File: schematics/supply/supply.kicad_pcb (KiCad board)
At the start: 4 copper layers, 237.5 x 175 mm, 293 parts, among them J1 Conn_01x02_Pin, J11 Conn_01x04_Pin, J13 USBASP, J14 USBASP, J15 Conn_01x05_Pin, J17 banana jack + fuse 20A, J18 Conn_02x04_Odd_Even, J19 banana jack + fuse 15A, J2 Conn_01x02_Pin, J20 jst xh angle, J21 jst xh angle, J3 Conn_01x01_Pin, J4 Conn_01x01_Pin, J5 CW2B-10A-T, J6 USB_A, J7 USB_A, J8 USB_A, J9 Conn_01x04_Pin, K1 SRD-12VDC-SL-C, M1 Fan, Q1 STP13NK60Z, Q10 IRLML0030, Q11 IRLML0030, Q12 IRLML0030, Q13 IRLML5203, Q14 IRLML5203, Q2 IRLML5203, Q3 40N06, Q4 STP13NK60Z, Q5 STP13NK60Z, Q6 IRLML0030, Q7 IRLML5203, Q8 IRLML5203, Q9 IRLML0030, SW3 SW_Push, U1 ICE2PCS01, U10 LM158DR, U11 IP2163, U12 LM158DR, U13 TL432DBZ, U14 LM158DR, U15 LDL1117S33R, U16 ATmega328-A, U17 ATtiny1616-M, U19 LM158DR, U2 TL331, U20 EL817, U21 IRS2153S, U22 TL331, U23 INA169, U24 LM1085-3.3, U25 INA3221, U3 R7731, U4 EL817, U5 TL432DBZ, U6 INA3221, U7 EL817, U8 MC34063AD, U9 IRS2153S, X1 CSX-750FCC, 16MHz, X2 HC-49U, 16MHz, Y1 B32022A3223M000

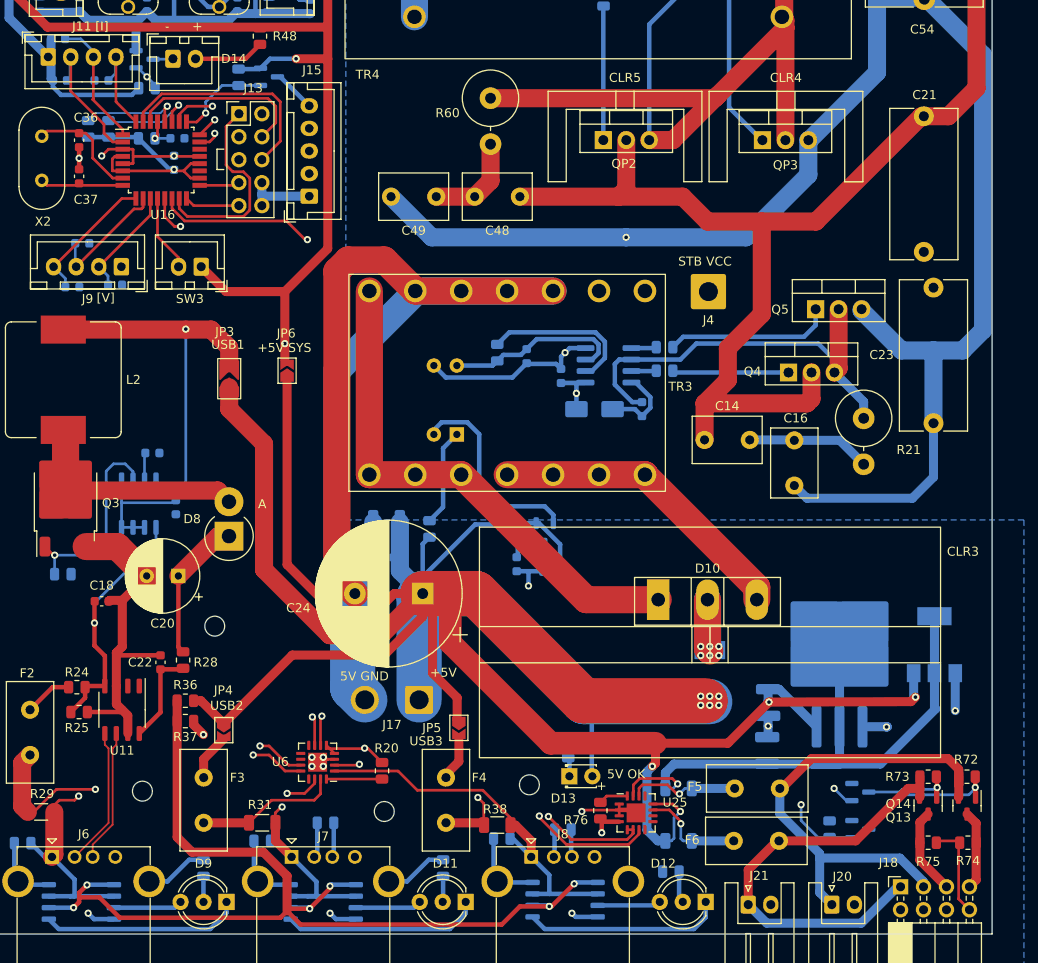
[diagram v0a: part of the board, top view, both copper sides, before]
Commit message: Added over-voltage protection to 5V line
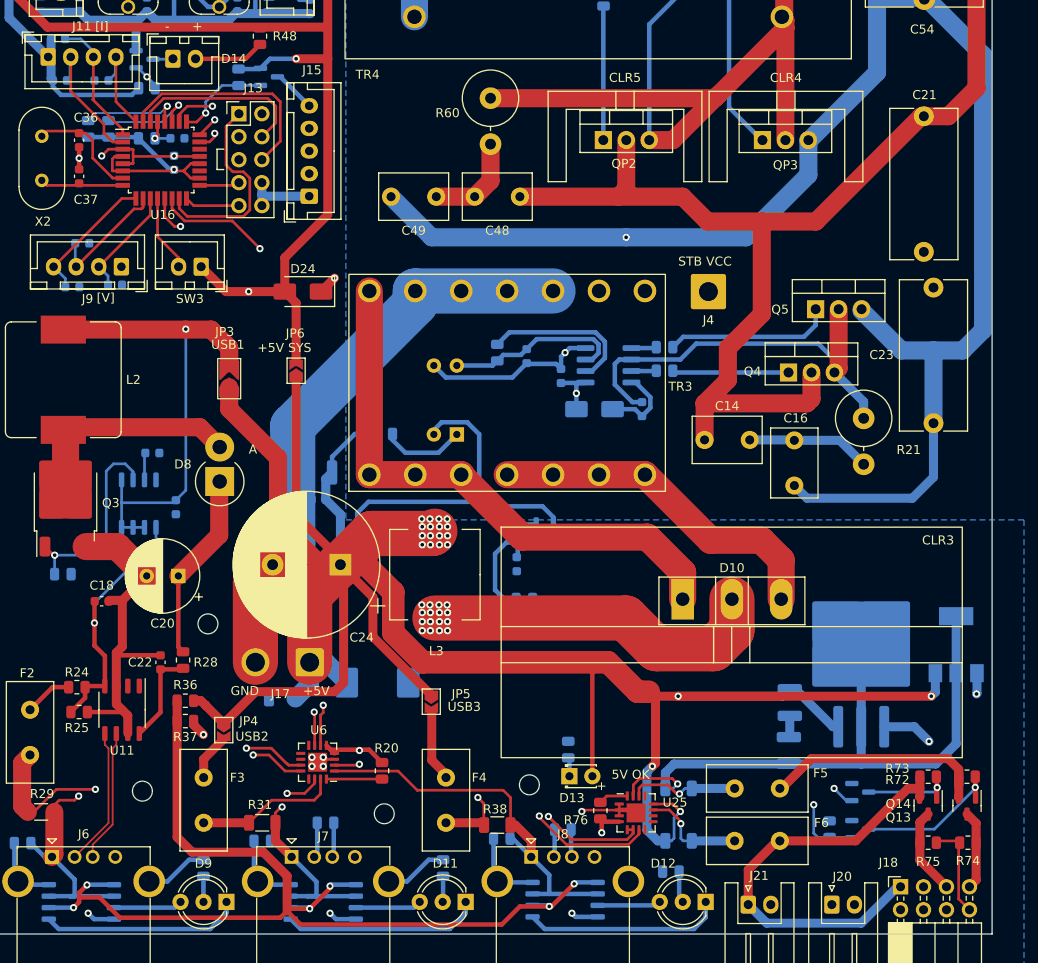
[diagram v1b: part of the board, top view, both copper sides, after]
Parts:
- added D24: SMAJ5.0CA-TR, Diode_SMD:D_SMA, F.Cu at (120.2, 164.8)
- added D25: SMCJ5.0A, Diode_SMD:D_SMC, B.Cu at (128.5, 208.0)
- added RV4: CT1206M6G, Resistor_SMD:R_1206_3216Metric, B.Cu at (118.0, 209.8)
- J17: value banana jack + fuse 20A -> banana jack + fuse 12A
- J19: value banana jack + fuse 15A -> banana jack + fuse 12A
- L3: value SPM6550T-2R2M -> HPI1040-1R0; footprint Inductor_SMD:L_Sumida_CDMC6D28_7.25x6.5mm -> Library:Ferrocore-HPI1040; moved to F.Cu
- moved L3 32.4 mm to (134.8, 196.1), turned to 90 degrees
- moved J17 12.8 mm to (121.0, 205.8)
- moved R19 11.6 mm to (129.2, 180.5), turned to 180 degrees
- moved C26 9.88 mm to (122.0, 187.8)
- moved C24 9.65 mm to (124.4, 194.9)
- moved C25 9.30 mm to (122.0, 184.8)
- moved D8 6.13 mm to (111.0, 185.8)
- moved R34 4.45 mm to (144.8, 198.8), turned to 0 degrees
- moved JP5 4.21 mm to (134.4, 210.1)
- moved D10 2.70 mm to (162.2, 198.8)
- moved C28 2.40 mm to (174.1, 210.2)
- moved C29 2.40 mm to (174.0, 215.5)
- moved CLR3 2.40 mm to (167.7, 203.8)
- moved U15 2.40 mm to (192.5, 203.8)
- moved U24 2.40 mm to (182.0, 205.2)
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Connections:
- net /Control & Fan/+5V renamed /Control & Fan/+5V_VSYS
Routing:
- net GND: track 1018.2 -> 920.6 mm, vias 17 -> 16
- net Net-(D10-K): track 23.0 -> 115.5 mm, vias 6 -> 16
- net /Internal 5V & out usb/+5V_OUT: track 375.7 -> 345.0 mm, vias 10 -> 20
- net /Control & Fan/+5V_VSYS: track 662.0 -> 671.1 mm
- net Net-(D10-A-Pad1): track 115.7 -> 124.7 mm
- net Net-(D10-A-Pad3): track 68.4 -> 77.1 mm
- net /Internal 5V & out usb/USB_1_BP: track 43.9 -> 48.8 mm
- net Net-(U13-REF): track 11.8 -> 15.4 mm
- net /Internal 5V & out usb/USB_3_+5V: track 4.49 -> 7.56 mm
- net /Control & Fan/SCL: track 177.1 -> 180.0 mm
- net /Internal 5V & out usb/+3.3_VOUT: track 68.2 -> 70.9 mm
- net /Control & Fan/SDA: track 183.4 -> 185.4 mm
- net Net-(R19-Pad1): track 10.8 -> 9.20 mm
- net /Control & Fan/SIGNAL_OUT: track 141.7 -> 140.3 mm
- net /Internal 5V & out usb/VBUS_3: track 42.5 -> 43.8 mm
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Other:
- board text removed: "5V GND"

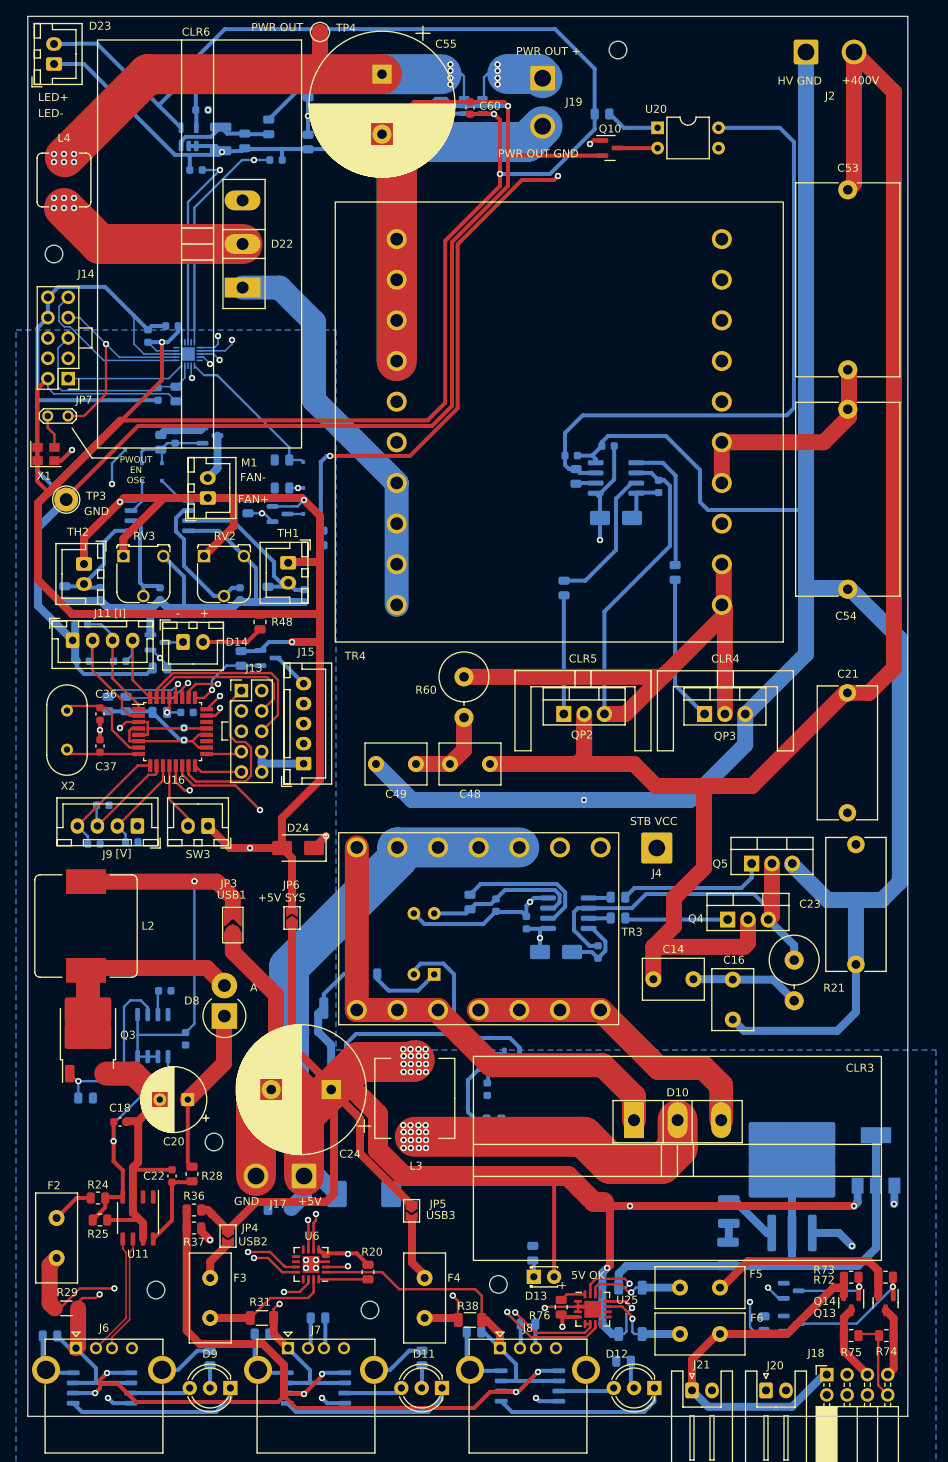
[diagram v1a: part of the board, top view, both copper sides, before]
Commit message: Fixed problem with 20V on one leg of comparator
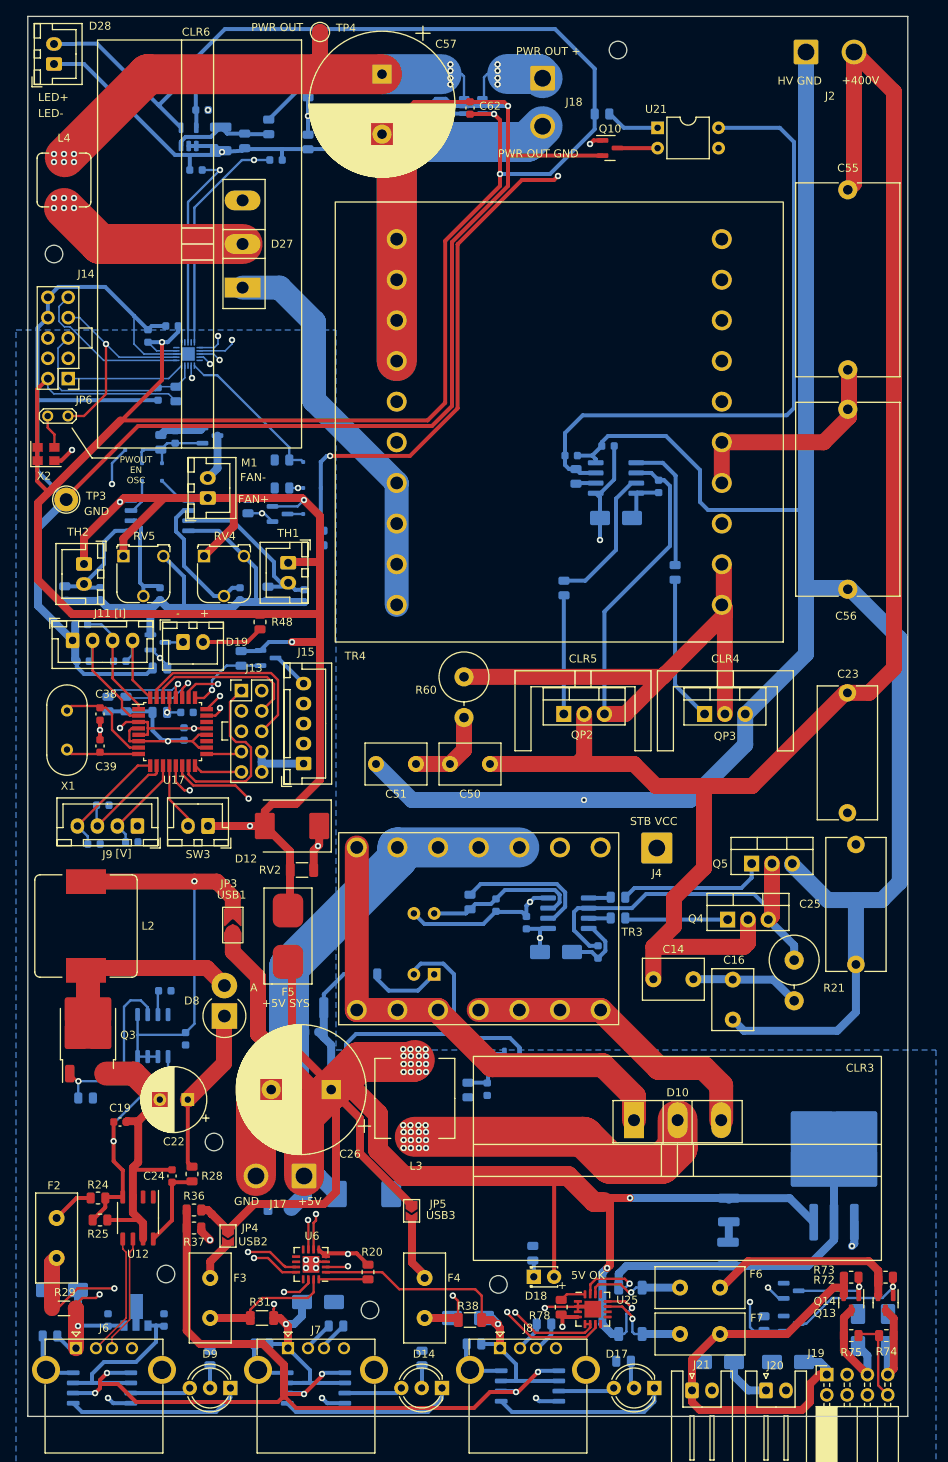
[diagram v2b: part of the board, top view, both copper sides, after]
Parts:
- removed the D24 at (120.2, 164.8)
- removed the JP6 at (119.5, 173.5)
- removed the U15 at (192.5, 203.8)
- added C18: 0.33 uF, Capacitor_SMD:C_0603_1608Metric, B.Cu at (96.5, 223.8)
- added C20: 0.1 uF, Capacitor_SMD:C_0603_1608Metric, B.Cu at (103.5, 223.8)
- added D11: SMAJ26A, Diode_SMD:D_SMA, B.Cu at (90.8, 220.0)
- added D12: SMCJ5.0A, Diode_SMD:D_SMC, F.Cu at (119.5, 162.0)
- added D13: SMAJ5.0CA-TR, Diode_SMD:D_SMA, B.Cu at (122.8, 221.5)
- added D15: SMAJ5.0CA-TR, Diode_SMD:D_SMA, B.Cu at (141.5, 223.5)
- added D29: SMAJ5.0CA-TR, Diode_SMD:D_SMA, B.Cu at (194.0, 225.0)
- added D30: SMAJ5.0CA-TR, Diode_SMD:D_SMA, B.Cu at (190.2, 225.0)
- added D31: SMAJ5.0CA-TR, Diode_SMD:D_SMA, B.Cu at (181.5, 229.0)
- added D32: SMAJ5.0CA-TR, Diode_SMD:D_SMA, B.Cu at (172.8, 229.0)
- added F5: 1808, 2A, Library:FuseHolder1808, F.Cu at (119.0, 175.8)
- added RV2: CT1206M6G, Resistor_SMD:R_1206_3216Metric, F.Cu at (120.8, 167.5)
- added U9: L78L33ACUTR, Package_TO_SOT_SMD:SOT-89-3, B.Cu at (100.0, 222.5)
- R1, R2, R3: value JNR10S500L -> JNR13S500L
- moved U16 5.42 mm to (187.2, 203.9)
- moved R34 4.96 mm to (141.5, 195.0), turned to -90 degrees
- moved R32 2.46 mm to (125.0, 224.5)
- moved H5 2.36 mm to (103.8, 218.0)
- moved R39 2.00 mm to (151.0, 224.2)
- moved R44 1.50 mm to (142.2, 226.8)
- moved R43 1.25 mm to (115.8, 226.8)
- moved R29 0.30 mm to (91.0, 222.3)
- moved C30 0.20 mm to (174.1, 210.0)
- renumbered C18 to C19, C19 to C21, C20 to C22, C21 to C23, C22 to C24, C23 to C25, C24 to C26, C25 to C27, C26 to C28, C27 to C29, C28 to C30, C29 to C31, C30 to C32, C31 to C33, C32 to C34, C33 to C35, C34 to C36, C35 to C37, C36 to C38, C37 to C39, C38 to C40, C39 to C41, C40 to C42, C41 to C43, C42 to C44, C43 to C45, C44 to C46, C45 to C47, C46 to C48, C47 to C49, C48 to C50, C49 to C51, C50 to C52, C51 to C53, C52 to C54, C53 to C55, C54 to C56, C55 to C57, C56 to C58, C57 to C59, C58 to C60, C59 to C61, C60 to C62, D11 to D14, D25 to D16, D12 to D17, D13 to D18, D14 to D19, D15 to D20, D16 to D21, D17 to D22, D18 to D23, D19 to D24, D20 to D25, D21 to D26, D22 to D27, D23 to D28, F5 to F6, F6 to F7, J19 to J18, J18 to J19, JP7 to JP6, R77 to R76, R78 to R77, R76 to R78, RV4 to RV3, RV2 to RV4, RV3 to RV5, U9 to U10, U10 to U11, U11 to U12, U12 to U13, U13 to U14, U14 to U15, U24 to U16, U16 to U17, U17 to U18, U19 to U20, U20 to U21, U21 to U22, U22 to U23, U23 to U24, X2 to X1, X1 to X2
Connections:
- U11 pad 3: /Internal 5V & out usb/VBUS_1 -> /Internal 5V & out usb/VBUS1_3.3V
- U11 pad 6: /Internal 5V & out usb/VBUS_1 -> /Internal 5V & out usb/VBUS1_3.3V
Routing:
- net /Internal 5V & out usb/+5V_OUT: track 345.0 -> 313.9 mm, vias 20 -> 19
- net /Internal 5V & out usb/VBUS1_3.3V: track 0.00 -> 21.9 mm
- net /Internal 5V & out usb/+3.3_VOUT: track 70.9 -> 50.0 mm
- net Net-(U14-REF): track 15.4 -> 7.97 mm
- net GND: track 920.6 -> 927.9 mm, vias 16 -> 15
- net /Output connectors/3.3V_FUSE: track 52.7 -> 59.2 mm
- net /Output connectors/5V_FUSE: track 47.7 -> 54.1 mm
- net /Control & Fan/+5V_VSYS: track 671.1 -> 677.0 mm
- net /Output connectors/SIGNAL_OUT_PWR_5V: track 9.63 -> 13.7 mm
- net /Internal 5V & out usb/VBUS_2: track 29.2 -> 33.3 mm, vias 2 -> 3
- net /Output connectors/SIGNAL_OUT_PWR_3V3: track 8.76 -> 12.1 mm
- net /Internal 5V & out usb/VBUS_1: track 52.5 -> 49.6 mm, vias 2 -> 3
- net /Internal 5V & out usb/VBUS_3: track 43.8 -> 45.8 mm, vias 0 -> 1
- net Net-(J8-D-): track 2.94 -> 3.78 mm
- net Net-(J8-D+): track 2.94 -> 3.72 mm
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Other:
- board text added: "Supply part1 v1.0"
- board text added: "Supply part2 v1.0"

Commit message: Some changes in board - Im preparing it to production
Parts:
- added H1: MountingHole, MountingHole:MountingHole_2.2mm_M2, F.Cu at (184.8, 225.0)
- F1: value 4A -> 1808, 4A
- F2: value JK30-300 -> 5A; footprint Capacitor_THT:C_Disc_D11.0mm_W5.0mm_P5.00mm -> Connector_Wire:SolderWire-0.75sqmm_1x02_P4.8mm_D1.25mm_OD2.3mm
- F3, F4, F6, F7: value JK30-200 -> 3A; footprint Capacitor_THT:C_Disc_D11.0mm_W5.0mm_P5.00mm -> Connector_Wire:SolderWire-0.75sqmm_1x02_P4.8mm_D1.25mm_OD2.3mm
- J15: value Conn_01x05_Pin -> Conn_01x06_Pin; footprint Connector_JST:JST_XH_B5B-XH-A_1x05_P2.50mm_Vertical -> Connector_JST:JST_XH_B6B-XH-A_1x06_P2.50mm_Vertical
- moved D16 13.3 mm to (117.6, 200.4), turned to 0 degrees
- moved J15 11.3 mm to (122.0, 143.0), turned to -90 degrees
- moved D31 11.0 mm to (170.5, 228.8)
- moved D32 6.75 mm to (179.5, 229.0)
- moved Q12 2.50 mm to (179.4, 220.1)
- moved Q11 2.30 mm to (179.6, 224.2)
- moved R71 2.30 mm to (176.2, 224.2)
- moved R48 1.25 mm to (115.5, 137.8)
- moved D24 1.12 mm to (98.8, 114.5)
- moved L2 1.06 mm to (94.1, 175.5)
- moved F7 1.00 mm to (168.1, 224.5)
- moved C49 0.86 mm to (105.8, 113.2)
- moved R58 0.80 mm to (103.2, 113.2)
- moved H6 0.60 mm to (104.2, 217.6)
- moved F3 0.46 mm to (109.5, 218.1)
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- renumbered H9 to H10, H1 to H2, H2 to H3, H3 to H4, H4 to H5, H5 to H6, H6 to H7, H7 to H8, H8 to H9
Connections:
- J15 pad 1: GND -> Net-(J15-Pin_1)
- J15 pad 5: Net-(J15-Pin_5) -> /Control & Fan/MISO
- J20 pad 1: /Output connectors/3.3V_FUSE -> GND
- J20 pad 2: GND -> /Output connectors/3.3V_FUSE
- J21 pad 1: /Output connectors/5V_FUSE -> GND
- J21 pad 2: GND -> /Output connectors/5V_FUSE
- Q7 pad 3: Net-(J15-Pin_5) -> Net-(J15-Pin_1)
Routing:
- net /Control & Fan/+5V_VSYS: track 677.0 -> 701.1 mm
- net /Control & Fan/TFT_DC: track 31.4 -> 17.3 mm
- net /Output connectors/5V_FUSE: track 54.1 -> 40.6 mm
- net /Control & Fan/MOSI: track 42.0 -> 30.2 mm
- net /Control & Fan/MISO: track 6.13 -> 15.2 mm
- net GND: track 927.9 -> 922.4 mm
- net Net-(D23-K): track 11.0 -> 15.8 mm
- net Net-(J15-Pin_1): track 0.00 -> 4.60 mm
- net Net-(J15-Pin_5): track 4.53 -> 0.00 mm
- net /Output connectors/3.3V_FUSE: track 59.2 -> 54.7 mm
- net /Control & Fan/SCK: track 16.6 -> 13.1 mm
- net /Control & Fan/SIGNAL_OUT: track 140.3 -> 136.9 mm
- net Net-(Q12-D): track 9.76 -> 12.6 mm
- net Net-(D8-A): track 24.6 -> 21.9 mm
- net Net-(Q11-D): track 16.0 -> 18.5 mm
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
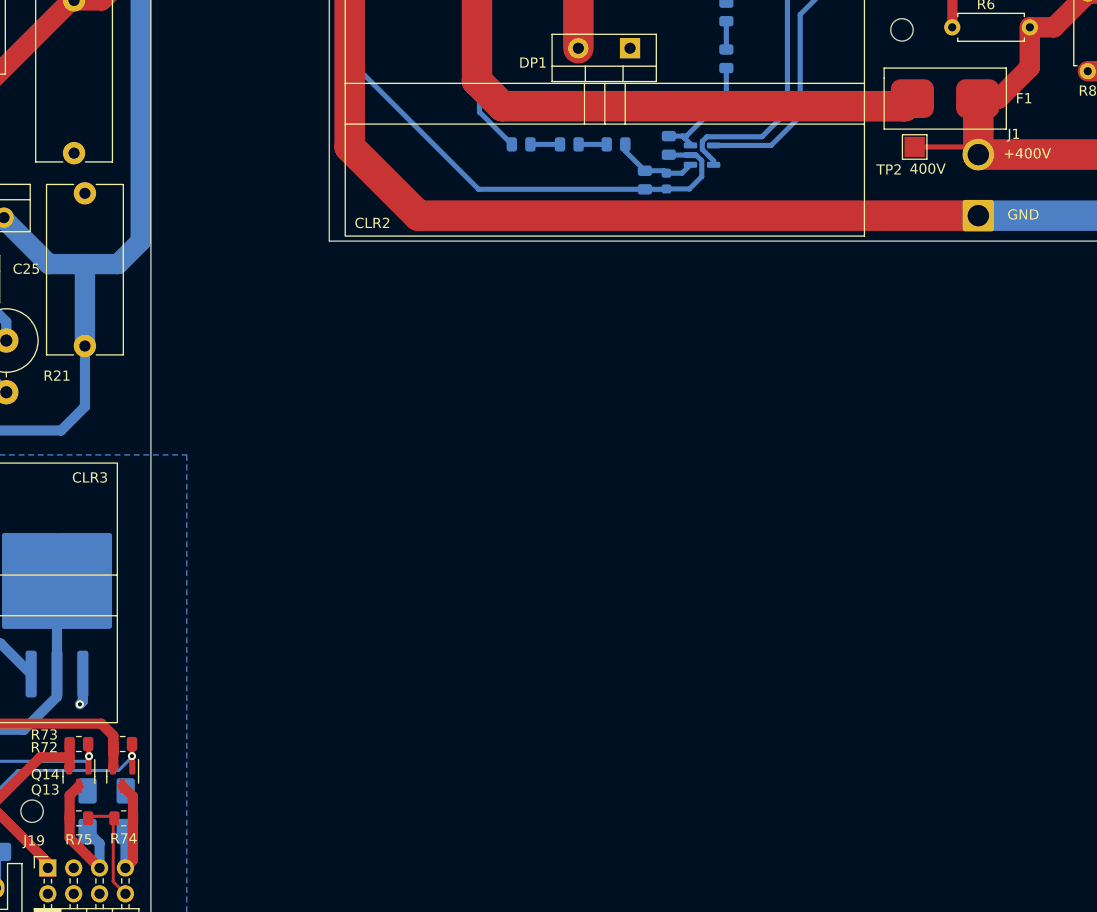
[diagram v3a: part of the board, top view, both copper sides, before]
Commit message: Changed fuse on 400V line
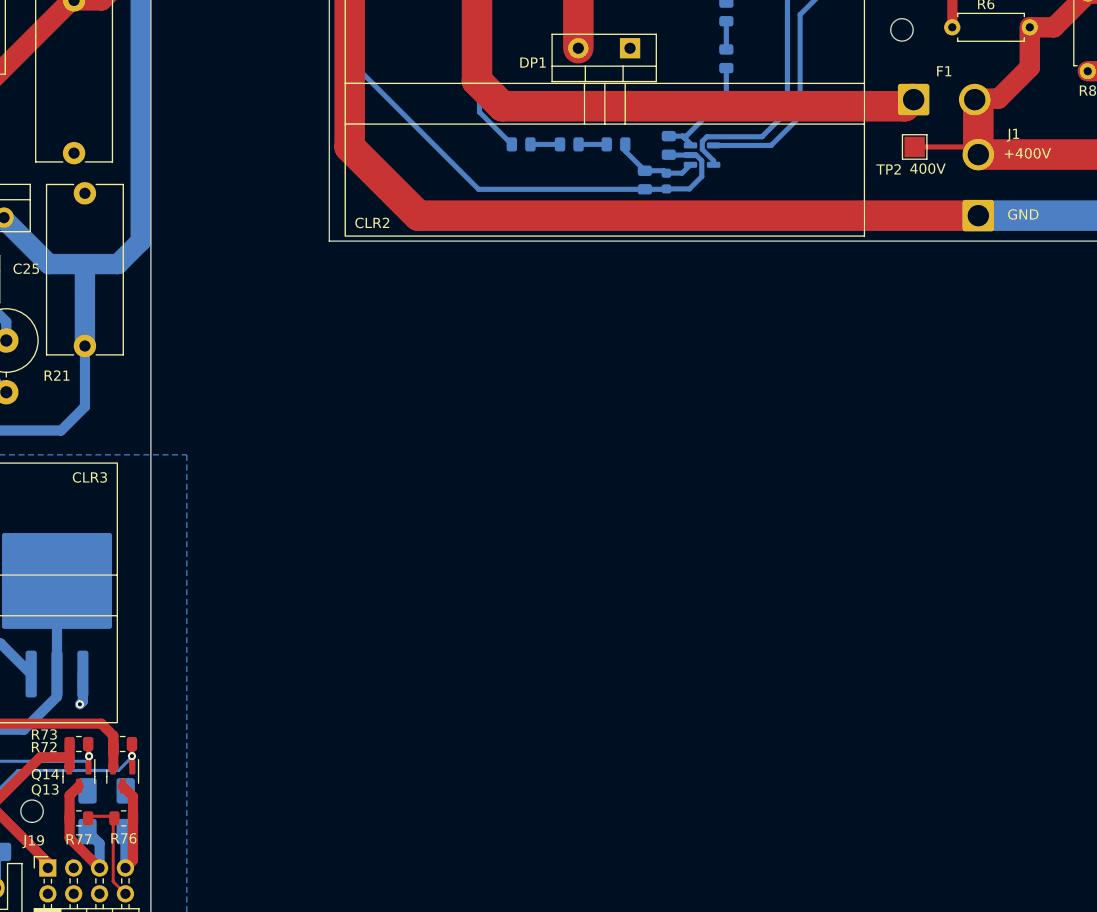
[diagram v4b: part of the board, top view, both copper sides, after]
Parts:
- F1: value 1808, 4A -> 10x38, 4A with fuseholder; footprint Library:FuseHolder1808 -> Connector_Wire:SolderWire-1.5sqmm_1x02_P6mm_D1.7mm_OD3mm
- J17, J18: value banana jack + fuse 12A -> banana jack + fuse 15A
- moved F1 3.10 mm to (271.4, 155.1)
- renumbered R76 to R74, R77 to R75, R74 to R76, R75 to R77
